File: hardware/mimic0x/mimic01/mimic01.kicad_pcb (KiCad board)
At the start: 2 copper layers, 35.6 x 20 mm, 33 parts, among them J2 Conn_01x06, J3 Conn_01x03, J5 Conn_01x05, Q1 AO3401A, SW1 TS-1088-AR02016, U1 PY32F071C1BU6TR_DIY

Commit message: Add hybrid open-source licenses (CERN-OHL-S, GPLv3, MIT)
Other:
- board text added: "© 2026 K. TAKAGI CERN-OHL-S-2.0"
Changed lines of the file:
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@@
 	)
 	(paper "A4")
+	(title_block
+		(comment 1 "License: CERN-OHL-S-2.0")
+		(comment 2 "Copyright (C) 2026 TAKAGI Katsuyuki")
+		(comment 3 "Project: Analog Mimic")
+	)
 	(layers
 		(0 "F.Cu" signal)
@@
 		)
 	)
+	(gr_text "© 2026 K. TAKAGI\nCERN-OHL-S-2.0"
+		(at 143.396 108.763 0)
+		(layer "B.SilkS")
+		(effects
+			(font
+				(size 0.8 0.8)
+				(thickness 0.12)
+			)
+			(justify left bottom mirror)
+		)
+	)

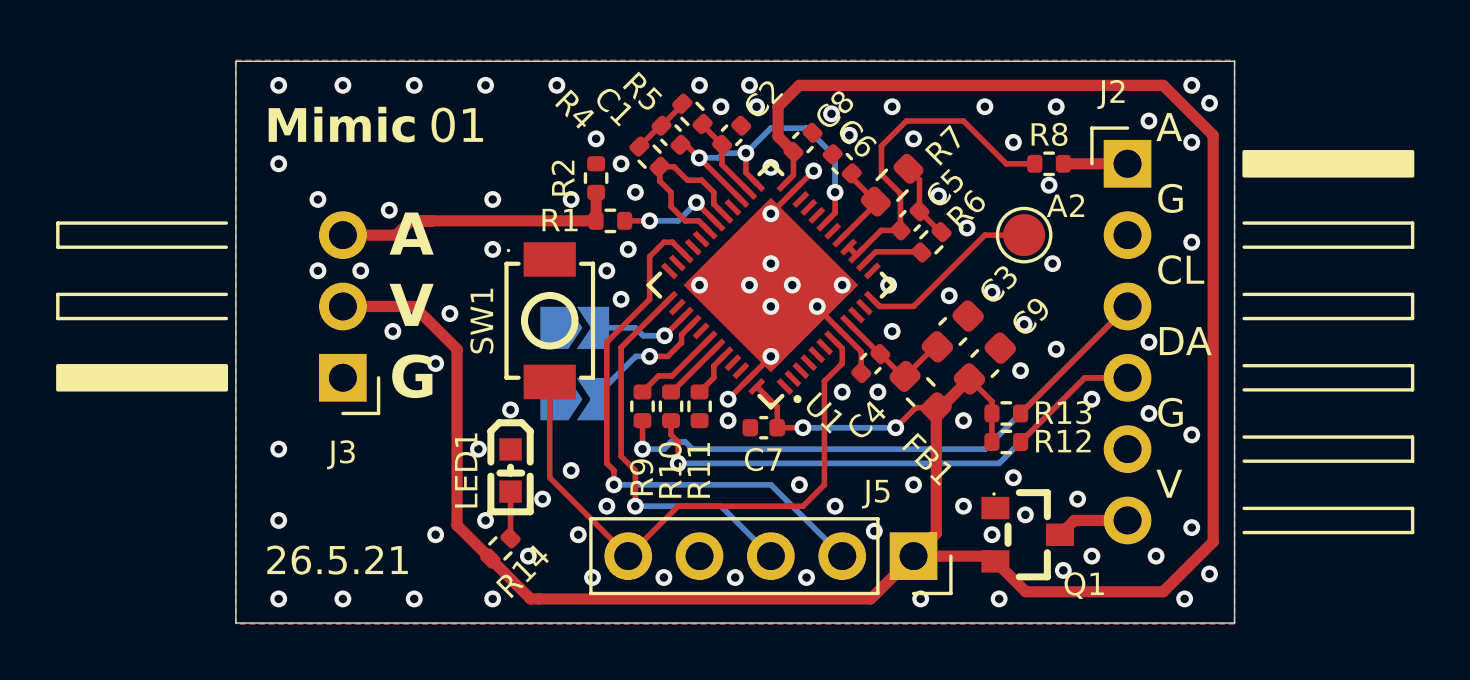
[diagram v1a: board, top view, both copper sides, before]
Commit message: Update silk and component values
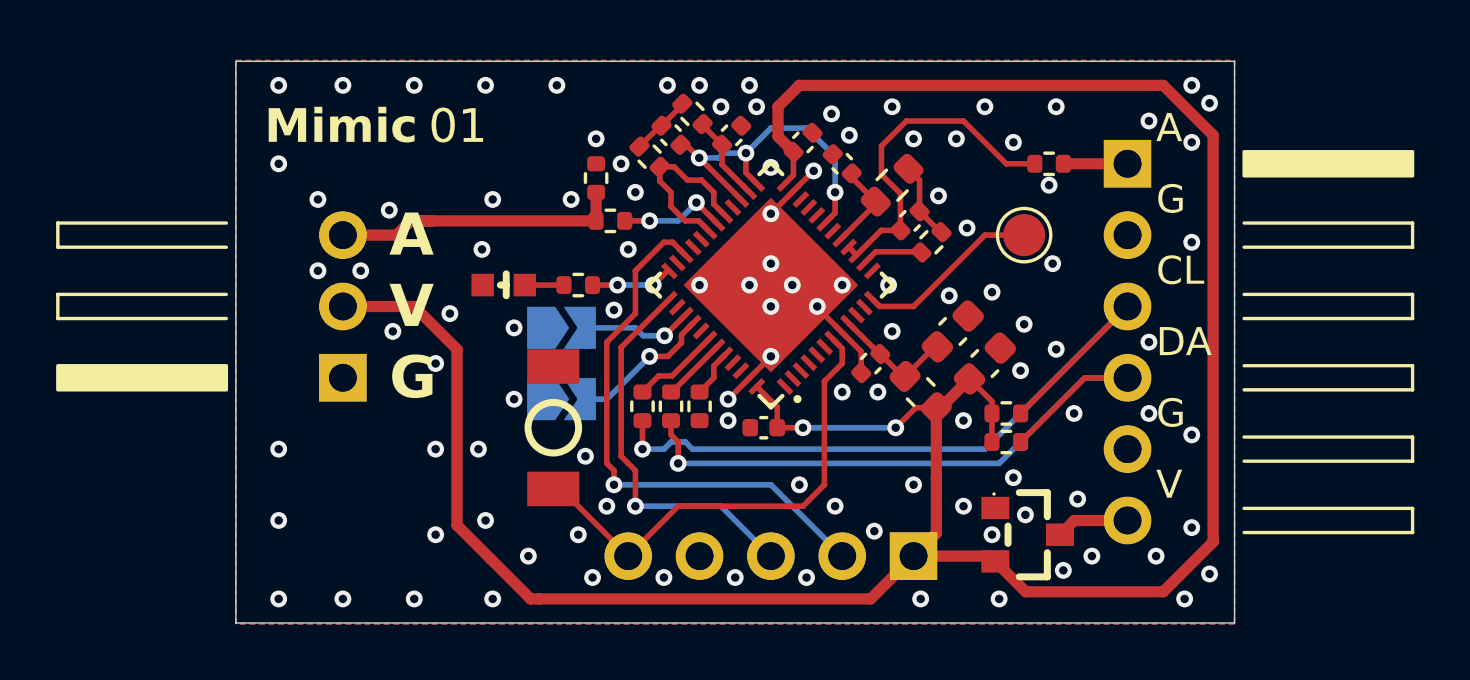
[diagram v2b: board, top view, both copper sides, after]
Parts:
- J5: footprint Connector_PinSocket_2.54mm:PinSocket_1x05_P2.54mm_Vertical -> EasyEDA:PinSocket_1x05_P2.54mm_Vertical_DIY
- moved R14 9.78 mm to (143.1, 98.0), turned to 0 degrees
- moved LED1 6.61 mm to (140.5, 98.0), turned to 0 degrees
- moved SW1 3.81 mm to (142.3, 103.0)
- moved JP1 0.47 mm to (142.5, 102.0)
- moved JP2 0.47 mm to (142.5, 99.5)
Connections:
- R14 pad 2: VCC -> Net-(U1-PF6)
- U1 pad 36: unconnected-(U1-PF6-Pad36) -> Net-(U1-PF6)
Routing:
- net /NRST: track 21.0 -> 17.3 mm
- net Net-(U1-PF6): track 0.00 -> 2.94 mm, vias 0 -> 2
- net GND: vias 105 -> 107
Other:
- board text added: "26.5.22"
- board text removed: "26.5.21"
- board text removed: "A2"
- board text removed: "SENSOR"
- board text removed: "by OtoHA"
